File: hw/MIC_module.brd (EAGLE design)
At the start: 25 x 45 mm, 35 parts, among them J1 GROVE-4P-2.0-3470130P1, J2 GROVE-4P-2.0-3470130P1

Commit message: added USB port
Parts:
- added J4: MICRO-USB-5P-340015001, OPL Eagle Library:B-SMD-5P
- added R11, R14: 22, rcl:R0603
- added R6: 100k, rcl:R0603
- added R8: 1k5, rcl:R0603
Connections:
- new net N$3: J4.2, R11.2
- new net N$32: J4.3, R14.2, R8.2
- new net N$5: J4.4, R6.2
- new net USB_N: R11.1, U$6.32
- new net USB_P: R14.1, U$6.33
- new net USB_VBUS: J4.1
- net +3V3: now also R8.1
- net GND: now also J4.5, J4.E1, J4.E2, J4.P1, J4.P2, R6.1
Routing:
- net N$32: track 0.00 -> 10.9 mm
- net N$3: track 0.00 -> 10.3 mm
- net +3V3: track 148.2 -> 155.2 mm
- net N$5: track 0.00 -> 6.56 mm
- net USB_P: track 0.00 -> 4.99 mm
- net USB_N: track 0.00 -> 3.00 mm
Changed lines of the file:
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@@
 <element name="R5" library="rcl" package="R0603" value="100" x="18.7" y="23.2" rot="R270"/>
 <element name="C15" library="rcl" package="C0603" value="15p" x="17.3" y="23.2" rot="R270"/>
+<element name="R11" library="rcl" package="R0603" value="22" x="7.8" y="17.2" rot="R90"/>
+<element name="R14" library="rcl" package="R0603" value="22" x="6.4" y="17.2" rot="R90"/>
+<element name="R6" library="rcl" package="R0603" value="100k" x="5" y="20.2" rot="R90"/>
+<element name="R8" library="rcl" package="R0603" value="1k5" x="5" y="17.2" rot="R90"/>
+<element name="J4" library="OPL Eagle Library" package="B-SMD-5P" value="MICRO-USB-5P-340015001" x="2.5" y="26" rot="R270"/>
 </elements>
 <signals>
@@
 <via x="23.4" y="44.1" extent="1-16" drill="0.3"/>
 <via x="24.1" y="43.4" extent="1-16" drill="0.3"/>
+<contactref element="J4" pad="5"/>
+<contactref element="J4" pad="E2"/>
+<contactref element="J4" pad="E1"/>
+<contactref element="J4" pad="P2"/>
+<contactref element="J4" pad="P1"/>
+<contactref element="R6" pad="1"/>
 </signal>
 <signal name="VIN">
@@
 <via x="18" y="34.5" extent="1-16" drill="0.3"/>
 <wire x1="18" y1="34.5" x2="18" y2="38.5" width="0.6" layer="16"/>
+<contactref element="R8" pad="1"/>
+<wire x1="5" y1="16.35" x2="4.35" y2="16.35" width="0.2" layer="1"/>
+<wire x1="4.35" y1="16.35" x2="4" y2="16.7" width="0.2" layer="1"/>
+<wire x1="4" y1="16.7" x2="4" y2="19.6" width="0.2" layer="1"/>
+<wire x1="4" y1="19.6" x2="3.4" y2="20.2" width="0.2" layer="1"/>
+<wire x1="3.4" y1="20.2" x2="2.56" y2="20.2" width="0.2" layer="1"/>
+<wire x1="2.56" y1="20.2" x2="1.7" y2="19.34" width="0.2" layer="1"/>
 </signal>
 <signal name="JTMS">
@@
 <wire x1="16.05" y1="20.75" x2="16.05" y2="19.55" width="0.2" layer="1"/>
 </signal>
+<signal name="USB_VBUS">
+<contactref element="J4" pad="1"/>
+</signal>
+<signal name="USB_N">
+<contactref element="R11" pad="1"/>
+<contactref element="U$6" pad="32"/>
+<wire x1="10.55" y1="15.75" x2="8.4" y2="15.75" width="0.2" layer="1"/>
+<wire x1="8.4" y1="15.75" x2="7.8" y2="16.35" width="0.2" layer="1"/>
+</signal>
+<signal name="USB_P">
+<contactref element="R14" pad="1"/>
+<contactref element="U$6" pad="33"/>
+<wire x1="10.55" y1="15.25" x2="6.85" y2="15.25" width="0.2" layer="1"/>
+<wire x1="6.85" y1="15.25" x2="6.4" y2="15.7" width="0.2" layer="1"/>
+<wire x1="6.4" y1="15.7" x2="6.4" y2="16.35" width="0.2" layer="1"/>
+</signal>
+<signal name="N$3">
+<contactref element="R11" pad="2"/>
+<contactref element="J4" pad="2"/>
+<wire x1="5.04" y1="26.65" x2="6.05" y2="26.65" width="0.2" layer="1"/>
+<wire x1="6.05" y1="26.65" x2="7.3" y2="25.4" width="0.2" layer="1"/>
+<wire x1="7.3" y1="25.4" x2="7.3" y2="19.3" width="0.2" layer="1"/>
+<wire x1="7.3" y1="19.3" x2="7.8" y2="18.8" width="0.2" layer="1"/>
+<wire x1="7.8" y1="18.8" x2="7.8" y2="18.05" width="0.2" layer="1"/>
+</signal>
+<signal name="N$32">
+<contactref element="R14" pad="2"/>
+<contactref element="R8" pad="2"/>
+<contactref element="J4" pad="3"/>
+<wire x1="5.04" y1="26" x2="6.1" y2="26" width="0.2" layer="1"/>
+<wire x1="6.1" y1="26" x2="6.9" y2="25.2" width="0.2" layer="1"/>
+<wire x1="6.9" y1="25.2" x2="6.9" y2="19.3" width="0.2" layer="1"/>
+<wire x1="6.9" y1="19.3" x2="6.4" y2="18.8" width="0.2" layer="1"/>
+<wire x1="6.4" y1="18.8" x2="6.4" y2="18.05" width="0.2" layer="1"/>
+<wire x1="5" y1="18.05" x2="6.4" y2="18.05" width="0.2" layer="1"/>
+</signal>
+<signal name="N$5">
+<contactref element="R6" pad="2"/>
+<contactref element="J4" pad="4"/>
+<wire x1="5" y1="21.05" x2="5.65" y2="21.05" width="0.2" layer="1"/>
+<wire x1="5.65" y1="21.05" x2="6.5" y2="21.9" width="0.2" layer="1"/>
+<wire x1="5.04" y1="25.35" x2="6.15" y2="25.35" width="0.2" layer="1"/>
+<wire x1="6.15" y1="25.35" x2="6.5" y2="25" width="0.2" layer="1"/>
+<wire x1="6.5" y1="25" x2="6.5" y2="21.9" width="0.2" layer="1"/>
+</signal>
 </signals>

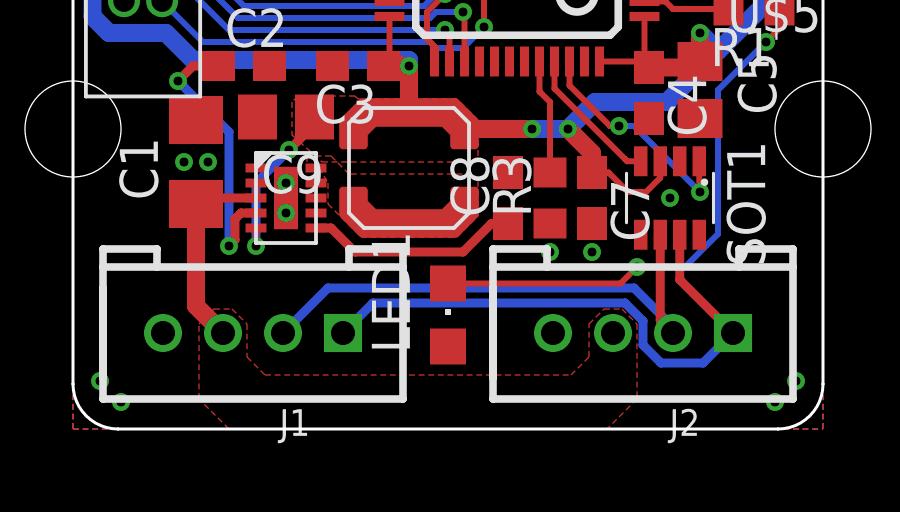
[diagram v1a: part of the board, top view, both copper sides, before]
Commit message: fixed led polarity
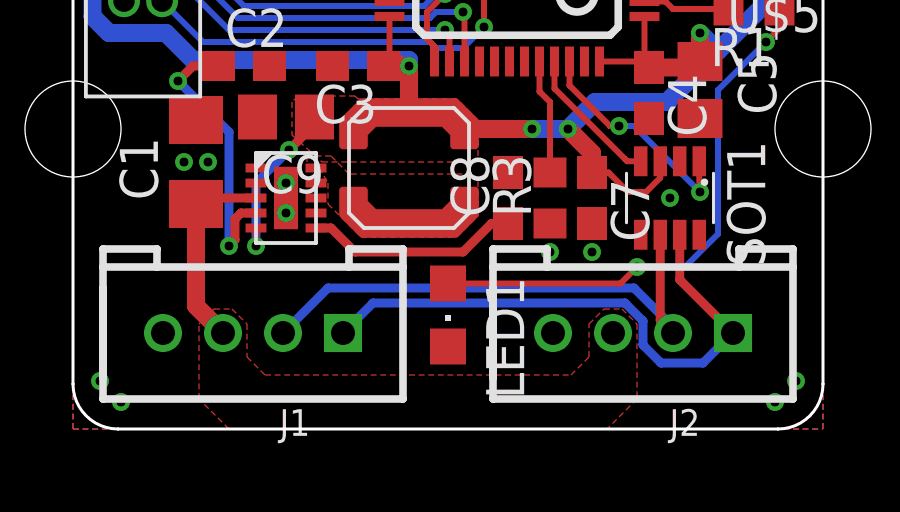
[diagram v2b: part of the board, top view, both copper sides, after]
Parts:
- turned LED1 to 180 degrees
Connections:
- net GND: now also LED1.C; no longer LED1.A
- net N$4: now also LED1.A; no longer LED1.C
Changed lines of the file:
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@@
 <layer number="42" name="bRestrict" color="1" fill="10" visible="no" active="yes"/>
 <layer number="43" name="vRestrict" color="2" fill="10" visible="no" active="yes"/>
-<layer number="44" name="Drills" color="7" fill="1" visible="yes" active="yes"/>
+<layer number="44" name="Drills" color="7" fill="1" visible="no" active="yes"/>
 <layer number="45" name="Holes" color="7" fill="1" visible="yes" active="yes"/>
 <layer number="46" name="Milling" color="3" fill="1" visible="yes" active="yes"/>
@@
 <layer number="49" name="Reference" color="7" fill="1" visible="no" active="yes"/>
 <layer number="50" name="dxf" color="7" fill="1" visible="no" active="no"/>
-<layer number="51" name="tDocu" color="7" fill="1" visible="no" active="yes"/>
+<layer number="51" name="tDocu" color="7" fill="1" visible="yes" active="yes"/>
 <layer number="52" name="bDocu" color="7" fill="1" visible="no" active="yes"/>
 <layer number="53" name="tGND_GNDA" color="7" fill="1" visible="no" active="no"/>
@@
 <element name="C3" library="rcl" package="C0603" value="100n" x="9.5" y="12.1" rot="R180"/>
 <element name="C7" library="rcl" package="C0603" value="100n" x="17.3" y="7.7" rot="R270"/>
-<element name="LED1" library="led" package="CHIPLED_0805" value="" x="12.5" y="3.8"/>
+<element name="LED1" library="led" package="CHIPLED_0805" value="" x="12.5" y="3.8" rot="R180"/>
 <element name="R1" library="rcl" package="R0603" value="330" x="22.7" y="14" rot="R180"/>
 <element name="U$4" library="samtec" package="FTSH-105-TH" value="FTSH-105TH" x="1.7" y="16.8" rot="R270"/>
@@
 <via x="7.1" y="8.2" extent="1-16" drill="0.3"/>
 <via x="7.1" y="7.2" extent="1-16" drill="0.3"/>
-<contactref element="LED1" pad="A"/>
 <contactref element="SOT1" pad="2"/>
 <contactref element="SOT1" pad="8"/>
@@
 <contactref element="J4" pad="P1"/>
 <contactref element="R6" pad="1"/>
+<contactref element="LED1" pad="C"/>
 </signal>
 <signal name="VIN">
@@
 <signal name="N$4">
 <contactref element="R1" pad="1"/>
-<contactref element="LED1" pad="C"/>
 <via x="23.1" y="12.9" extent="1-16" drill="0.3"/>
 <wire x1="23.55" y1="14" x2="23.55" y2="13.35" width="0.2" layer="1"/>
 <wire x1="23.55" y1="13.35" x2="23.1" y2="12.9" width="0.2" layer="1"/>
-<wire x1="12.5" y1="4.85" x2="18.25" y2="4.85" width="0.2" layer="1"/>
 <wire x1="18.25" y1="4.85" x2="18.8" y2="5.4" width="0.2" layer="1"/>
 <via x="18.8" y="5.4" extent="1-16" drill="0.3"/>
@@
 <wire x1="21.5" y1="6.5" x2="21.5" y2="11.3" width="0.2" layer="16"/>
 <wire x1="21.5" y1="11.3" x2="23.1" y2="12.9" width="0.2" layer="16"/>
+<contactref element="LED1" pad="A"/>
+<wire x1="12.5" y1="4.85" x2="18.25" y2="4.85" width="0.2" layer="1"/>
 </signal>
 <signal name="N$2">
